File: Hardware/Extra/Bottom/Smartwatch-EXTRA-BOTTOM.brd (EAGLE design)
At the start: 33 x 33 mm, 46 parts, among them U1 AD5242-SO16, U2 PCF8523, U3 AD5171

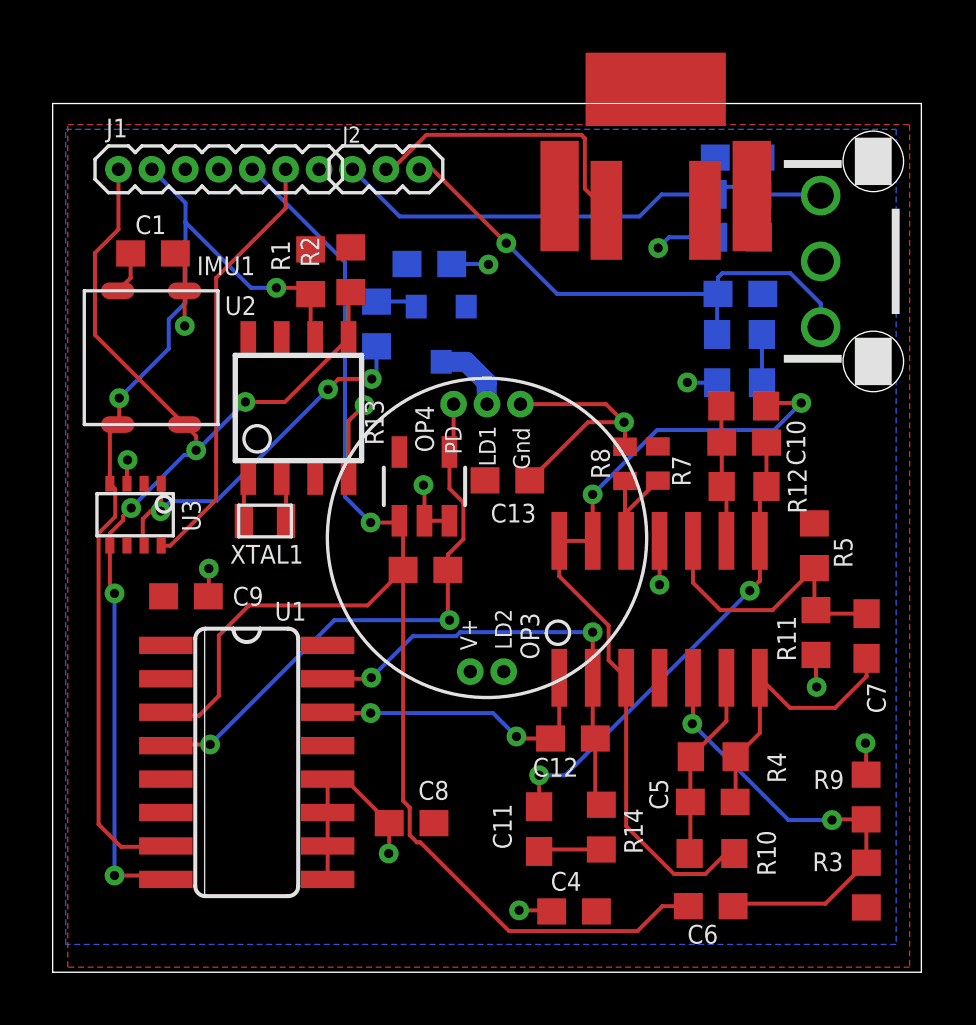
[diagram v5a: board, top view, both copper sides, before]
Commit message: Silkscreens fixed, Airwires removed
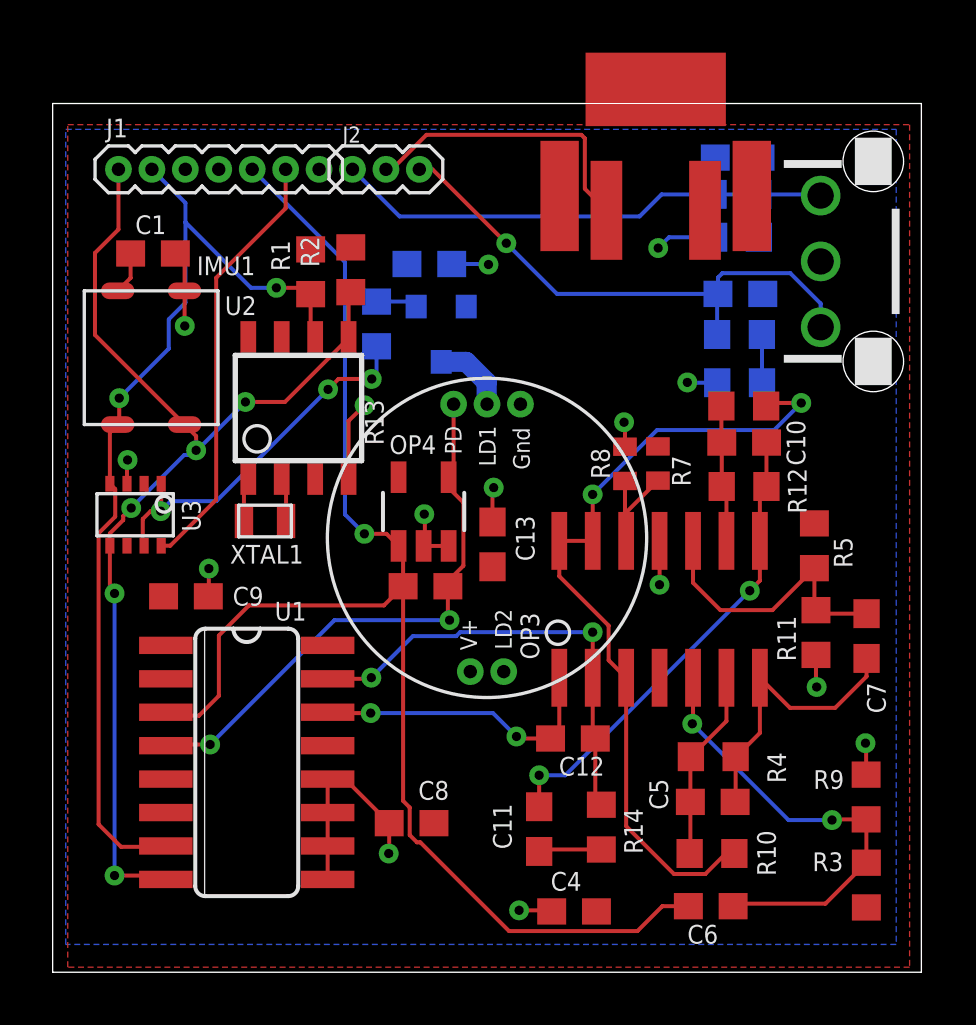
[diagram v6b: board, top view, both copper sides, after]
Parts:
- moved C13 2.50 mm to (19.2, 18.8), turned to 270 degrees
- moved OP4 0.96 mm to (16.6, 20.0)
- moved C3 0.62 mm to (16.7, 17.2)
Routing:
- net GND: track 33.2 -> 25.7 mm, vias 11 -> 12
